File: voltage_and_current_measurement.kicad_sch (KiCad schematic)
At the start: 86 parts, among them IC2 VIA2000SD, J5 V_bat_in, J6 V_bat_out, J7 V_bat_in, J8 V_bat_out, U2 ACS37030LLZATR-065B3, U3 CZ3A05, U4 OPA2328DR, U5 OPA2328DR

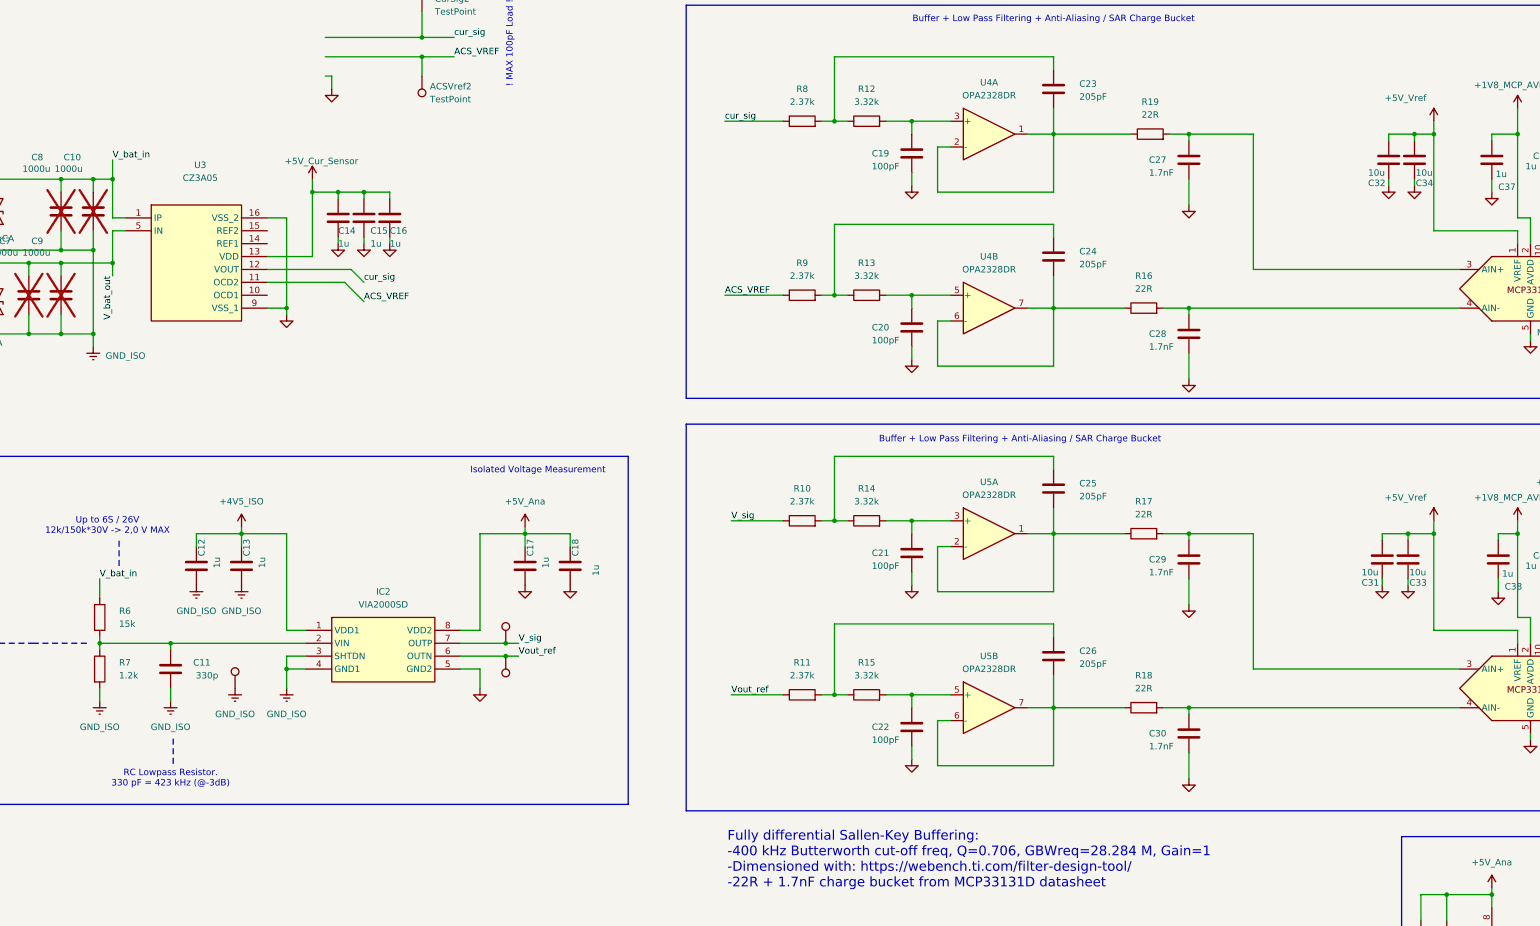
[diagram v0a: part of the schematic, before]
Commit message: Implemented dual SAR ADC Buffering and Current sensor ratiometric supply
[KiCad Version: 10.0.4]
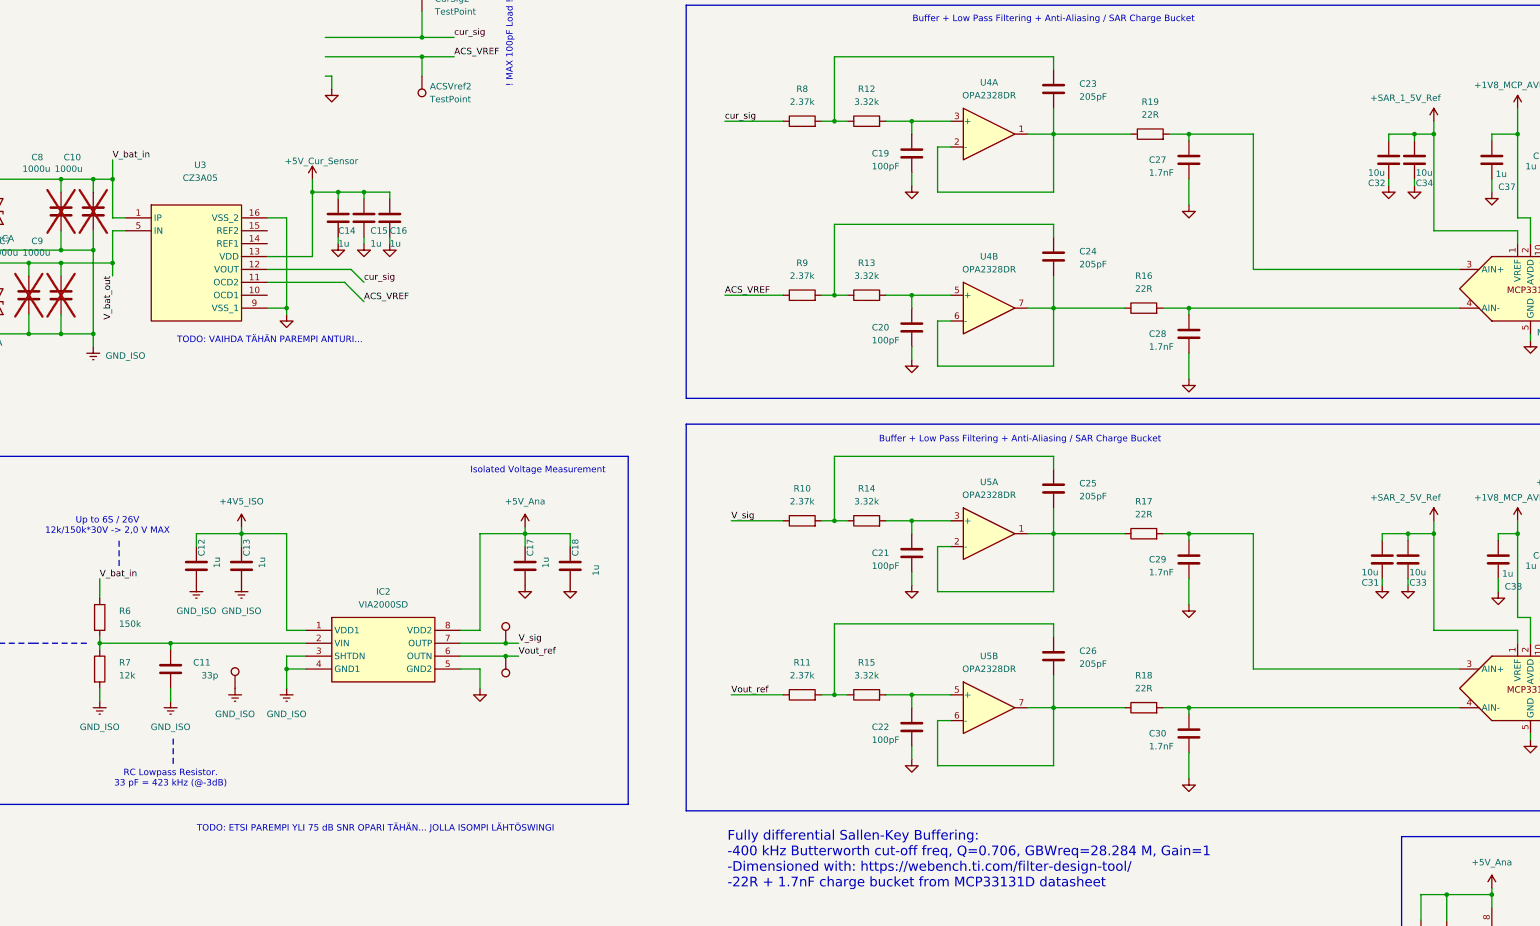
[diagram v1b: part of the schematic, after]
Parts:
- C11: value 330p -> 33p
- R6: value 15k -> 150k
- R7: value 1.2k -> 12k
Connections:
- net +5V_Vref renamed +SAR_1_5V_Ref
- net +SAR_1_5V_Ref: no longer C31.1, C33.1, MCP2.1 (VREF)
- new net +SAR_2_5V_Ref: C31.1, C33.1, MCP2.1 (VREF)
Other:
- note added: "RC Lowpass Resistor. 33 pF = 423 kHz (@-3dB)"
- note added: "TODO: ETSI PAREMPI YLI 75 dB SNR OPARI TÄHÄN... JOLLA ISOMPI LÄHTÖSWINGI"
- note added: "TODO: VAIHDA TÄHÄN PAREMPI ANTURI..."
- note removed: "RC Lowpass Resistor. 330 pF = 423 kHz (@-3dB)"
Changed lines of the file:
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@@
 		)
 	)
-	(text "RC Lowpass Resistor.\n330 pF = 423 kHz (@-3dB)\n"
+	(text "RC Lowpass Resistor.\n33 pF = 423 kHz (@-3dB)\n"
 		(exclude_from_sim no)
 		(at 77.47 193.04 0)
@@
 		)
 	)
+	(text "TODO: VAIHDA TÄHÄN PAREMPI ANTURI..."
+		(exclude_from_sim no)
+		(at 97.028 106.68 0)
+		(effects
+			(font
+				(size 1.27 1.27)
+			)
+		)
+	)
 	(text "Up to 6S / 26V\n12k/150k*30V -> 2,0 V MAX"
 		(exclude_from_sim no)
@@
 		)
 	)
+	(text "TODO: ETSI PAREMPI YLI 75 dB SNR OPARI TÄHÄN... JOLLA ISOMPI LÄHTÖSWINGI"
+		(exclude_from_sim no)
+		(at 117.856 202.946 0)
+		(effects
+			(font
+				(size 1.27 1.27)
+			)
+		)
+	)
 	(text "! MAX 100pF Load !"
 		(exclude_from_sim no)
@@
 	(symbol
 		(lib_id "power:+3V3")
-		(at 326.39 142.24 0)
+		(at 326.39 63.5 0)
 		(unit 1)
 		(body_style 1)
@@
 		(in_pos_files yes)
 		(dnp no)
-		(property "Reference" "#PWR048"
-			(at 326.39 146.05 0)
+		(property "Reference" "#PWR047"
+			(at 326.39 67.31 0)
 			(hide yes)
 			(show_name no)
@@
 			)
 		)
-		(property "Value" "+5V_Vref"
-			(at 320.802 137.668 0)
+		(property "Value" "+SAR_1_5V_Ref"
+			(at 320.802 58.928 0)
 			(show_name no)
 			(do_not_autoplace no)
@@
 		)
 		(property "Footprint" ""
-			(at 326.39 142.24 0)
+			(at 326.39 63.5 0)
 			(hide yes)
 			(show_name no)
@@
 		)
 		(property "Datasheet" ""
-			(at 326.39 142.24 0)
+			(at 326.39 63.5 0)
 			(hide yes)
 			(show_name no)
@@
 		)
 		(property "Description" "Power symbol creates a global label with name \"+3V3\""
-			(at 326.39 142.24 0)
+			(at 326.39 63.5 0)
 			(hide yes)
 			(show_name no)
@@
 			(project "motor_testbench_v1_0"
 				(path "/da638649-102c-44f9-b928-e91cd399cc2f/2da1fd24-7545-4e4a-b589-72e0f66a31f4"
-					(reference "#PWR048")
+					(reference "#PWR047")
 					(unit 1)
 				)
@@
 			)
 		)
-		(property "Value" "330p"
+		(property "Value" "33p"
 			(at 86.868 172.72 0)
 			(show_name no)
@@
 			)
 		)
-		(property "Value" "1.2k"
+		(property "Value" "12k"
 			(at 67.31 172.7199 0)
 			(show_name no)
@@
 	)
 	(symbol
-		(lib_id "power:+3V3")
-		(at 326.39 63.5 0)
-		(unit 1)
-		(body_style 1)
-		(exclude_from_sim no)
-		(in_bom yes)
-		(on_board yes)
-		(in_pos_files yes)
-		(dnp no)
-		(property "Reference" "#PWR047"
-			(at 326.39 67.31 0)
-			(hide yes)
-			(show_name no)
-			(do_not_autoplace no)
-			(effects
-				(font
-					(size 1.27 1.27)
-				)
-			)
-		)
-		(property "Value" "+5V_Vref"
-			(at 320.802 58.928 0)
-			(show_name no)
-			(do_not_autoplace no)
-			(effects
-				(font
-					(size 1.27 1.27)
-				)
-			)
-		)
-		(property "Footprint" ""
-			(at 326.39 63.5 0)
-			(hide yes)
-			(show_name no)
-			(do_not_autoplace no)
-			(effects
-				(font
-					(size 1.27 1.27)
-				)
-			)
-		)
-		(property "Datasheet" ""
-			(at 326.39 63.5 0)
-			(hide yes)
-			(show_name no)
-			(do_not_autoplace no)
-			(effects
-				(font
-					(size 1.27 1.27)
-				)
-			)
-		)
-		(property "Description" "Power symbol creates a global label with name \"+3V3\""
-			(at 326.39 63.5 0)
-			(hide yes)
-			(show_name no)
-			(do_not_autoplace no)
-			(effects
-				(font
-					(size 1.27 1.27)
-				)
-			)
-		)
-		(pin "1"
-		)
-		(instances
-			(project "motor_testbench_v1_0"
-				(path "/da638649-102c-44f9-b928-e91cd399cc2f/2da1fd24-7545-4e4a-b589-72e0f66a31f4"
-					(reference "#PWR047")
-					(unit 1)
-				)
-			)
-		)
-	)
-	(symbol
 		(lib_id "Device:C")
 		(at -40.64 43.18 0)
@@
 			)
 		)
-		(property "Value" "15k"
+		(property "Value" "150k"
 			(at 67.31 162.5599 0)
 			(show_name no)
@@
 					(unit 1)
 				)
+			)
+		)
+	)
+	(symbol
+		(lib_id "power:+3V3")
+		(at 326.39 142.24 0)
+		(unit 1)
+		(body_style 1)
+		(exclude_from_sim no)
+		(in_bom yes)
+		(on_board yes)
+		(in_pos_files yes)
+		(dnp no)
+		(property "Reference" "#PWR048"
+			(at 326.39 146.05 0)
+			(hide yes)
+			(show_name no)
+			(do_not_autoplace no)
+			(effects
+				(font
+					(size 1.27 1.27)
+				)
+			)
+		)
+		(property "Value" "+SAR_2_5V_Ref"
+			(at 320.802 137.668 0)
+			(show_name no)
+			(do_not_autoplace no)
+			(effects
+				(font
+					(size 1.27 1.27)
+				)
+			)
+		)
+		(property "Footprint" ""
+			(at 326.39 142.24 0)
+			(hide yes)
+			(show_name no)
+			(do_not_autoplace no)
+			(effects
+				(font
+					(size 1.27 1.27)
+				)
+			)
+		)
+		(property "Datasheet" ""
+			(at 326.39 142.24 0)
+			(hide yes)
+			(show_name no)
+			(do_not_autoplace no)
+			(effects
+				(font
+					(size 1.27 1.27)
+				)
+			)
+		)
+		(property "Description" "Power symbol creates a global label with name \"+3V3\""
+			(at 326.39 142.24 0)
+			(hide yes)
+			(show_name no)
+			(do_not_autoplace no)
+			(effects
+				(font
+					(size 1.27 1.27)
+				)
+			)
+		)
+		(pin "1"
+		)
+		(instances
+			(project "motor_testbench_v1_0"
+				(path "/da638649-102c-44f9-b928-e91cd399cc2f/2da1fd24-7545-4e4a-b589-72e0f66a31f4"
+					(reference "#PWR048")
+					(unit 1)
+				)

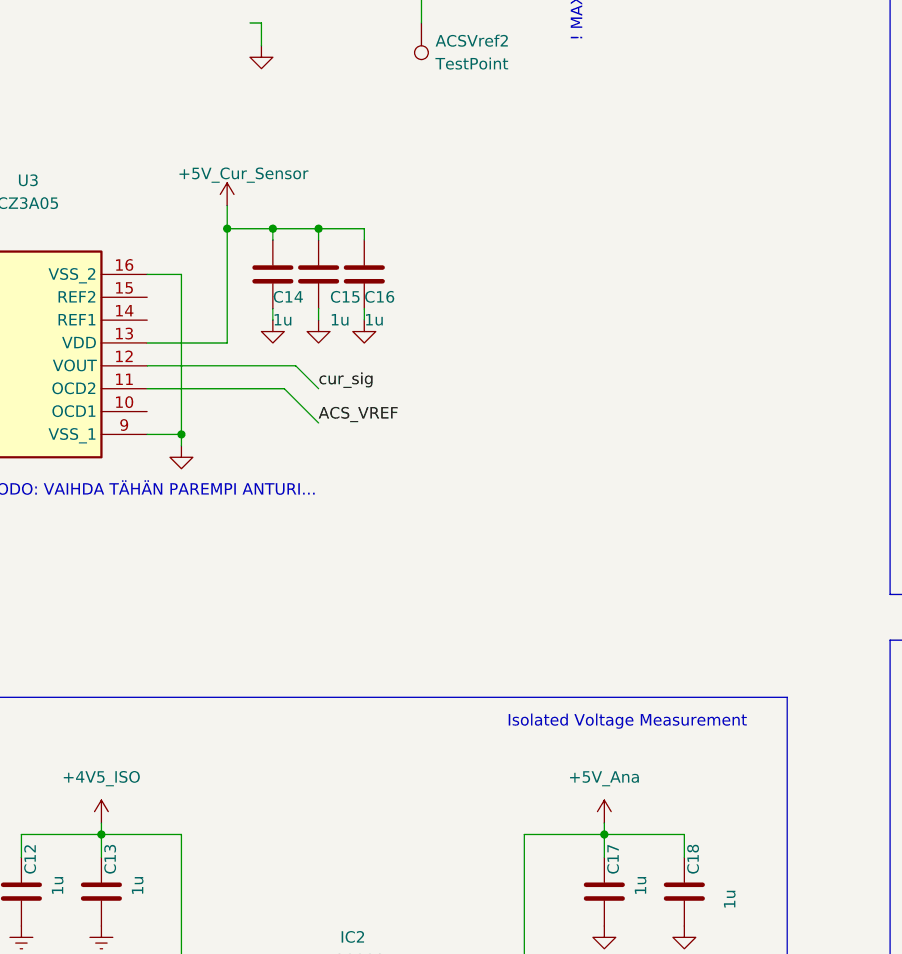
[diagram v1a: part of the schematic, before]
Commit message: Improved NTC measurements, improved layout. Added proper startup sequence for the power stages.
[KiCad Version: 10.0.4]
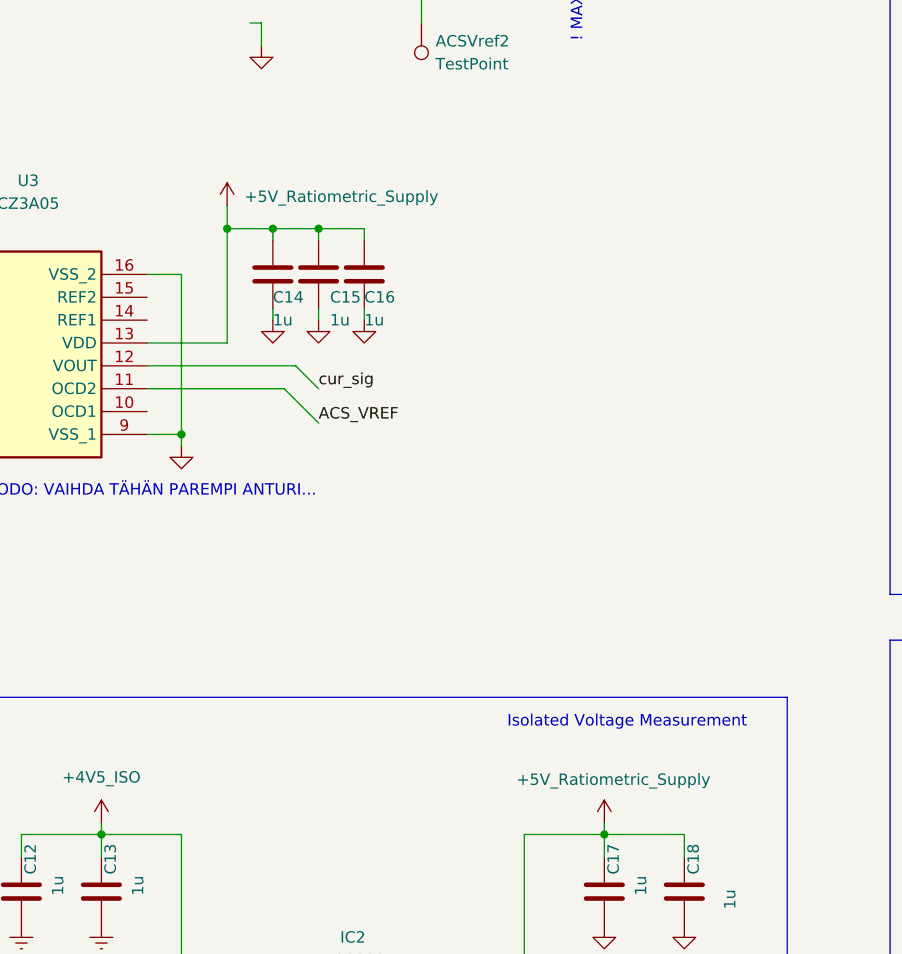
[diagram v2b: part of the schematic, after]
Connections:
- net +5V_Ana: no longer C17.1, C18.1, IC2.8 (VDD2)
- net +5V_Cur_Sensor renamed +5V_Ratiometric_Supply
- net +5V_Ratiometric_Supply: now also C17.1, C18.1, IC2.8 (VDD2)
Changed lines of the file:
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@@
 	)
 	(symbol
-		(lib_id "power:+3V3")
-		(at 147.32 143.51 0)
-		(unit 1)
-		(body_style 1)
-		(exclude_from_sim no)
-		(in_bom yes)
-		(on_board yes)
-		(in_pos_files yes)
-		(dnp no)
-		(property "Reference" "#PWR031"
-			(at 147.32 147.32 0)
-			(hide yes)
-			(show_name no)
-			(do_not_autoplace no)
-			(effects
-				(font
-					(size 1.27 1.27)
-				)
-			)
-		)
-		(property "Value" "+5V_Ana"
-			(at 147.32 138.43 0)
-			(show_name no)
-			(do_not_autoplace no)
-			(effects
-				(font
-					(size 1.27 1.27)
-				)
-			)
-		)
-		(property "Footprint" ""
-			(at 147.32 143.51 0)
-			(hide yes)
-			(show_name no)
-			(do_not_autoplace no)
-			(effects
-				(font
-					(size 1.27 1.27)
-				)
-			)
-		)
-		(property "Datasheet" ""
-			(at 147.32 143.51 0)
-			(hide yes)
-			(show_name no)
-			(do_not_autoplace no)
-			(effects
-				(font
-					(size 1.27 1.27)
-				)
-			)
-		)
-		(property "Description" "Power symbol creates a global label with name \"+3V3\""
-			(at 147.32 143.51 0)
-			(hide yes)
-			(show_name no)
-			(do_not_autoplace no)
-			(effects
-				(font
-					(size 1.27 1.27)
-				)
-			)
-		)
-		(pin "1"
-		)
-		(instances
-			(project "motor_testbench_v1_0"
-				(path "/da638649-102c-44f9-b928-e91cd399cc2f/2da1fd24-7545-4e4a-b589-72e0f66a31f4"
-					(reference "#PWR031")
-					(unit 1)
-				)
-			)
-		)
-	)
-	(symbol
 		(lib_id "Connector:TestPoint")
 		(at 365.76 163.83 0)
@@
 	)
 	(symbol
+		(lib_id "power:+3V3")
+		(at 105.41 74.93 0)
+		(unit 1)
+		(body_style 1)
+		(exclude_from_sim no)
+		(in_bom yes)
+		(on_board yes)
+		(in_pos_files yes)
+		(dnp no)
+		(property "Reference" "#PWR025"
+			(at 105.41 78.74 0)
+			(hide yes)
+			(show_name no)
+			(do_not_autoplace no)
+			(effects
+				(font
+					(size 1.27 1.27)
+				)
+			)
+		)
+		(property "Value" "+5V_Ratiometric_Supply"
+			(at 118.11 73.914 0)
+			(show_name no)
+			(do_not_autoplace no)
+			(effects
+				(font
+					(size 1.27 1.27)
+				)
+			)
+		)
+		(property "Footprint" ""
+			(at 105.41 74.93 0)
+			(hide yes)
+			(show_name no)
+			(do_not_autoplace no)
+			(effects
+				(font
+					(size 1.27 1.27)
+				)
+			)
+		)
+		(property "Datasheet" ""
+			(at 105.41 74.93 0)
+			(hide yes)
+			(show_name no)
+			(do_not_autoplace no)
+			(effects
+				(font
+					(size 1.27 1.27)
+				)
+			)
+		)
+		(property "Description" "Power symbol creates a global label with name \"+3V3\""
+			(at 105.41 74.93 0)
+			(hide yes)
+			(show_name no)
+			(do_not_autoplace no)
+			(effects
+				(font
+					(size 1.27 1.27)
+				)
+			)
+		)
+		(pin "1"
+		)
+		(instances
+			(project "motor_testbench_v1_0"
+				(path "/da638649-102c-44f9-b928-e91cd399cc2f/2da1fd24-7545-4e4a-b589-72e0f66a31f4"
+					(reference "#PWR025")
+					(unit 1)
+				)
+			)
+		)
+	)
+	(symbol
 		(lib_id "power:GND")
 		(at -40.64 48.26 0)
@@
 	)
 	(symbol
+		(lib_id "power:+3V3")
+		(at 147.32 143.51 0)
+		(unit 1)
+		(body_style 1)
+		(exclude_from_sim no)
+		(in_bom yes)
+		(on_board yes)
+		(in_pos_files yes)
+		(dnp no)
+		(property "Reference" "#PWR031"
+			(at 147.32 147.32 0)
+			(hide yes)
+			(show_name no)
+			(do_not_autoplace no)
+			(effects
+				(font
+					(size 1.27 1.27)
+				)
+			)
+		)
+		(property "Value" "+5V_Ratiometric_Supply"
+			(at 148.336 138.684 0)
+			(show_name no)
+			(do_not_autoplace no)
+			(effects
+				(font
+					(size 1.27 1.27)
+				)
+			)
+		)
+		(property "Footprint" ""
+			(at 147.32 143.51 0)
+			(hide yes)
+			(show_name no)
+			(do_not_autoplace no)
+			(effects
+				(font
+					(size 1.27 1.27)
+				)
+			)
+		)
+		(property "Datasheet" ""
+			(at 147.32 143.51 0)
+			(hide yes)
+			(show_name no)
+			(do_not_autoplace no)
+			(effects
+				(font
+					(size 1.27 1.27)
+				)
+			)
+		)
+		(property "Description" "Power symbol creates a global label with name \"+3V3\""
+			(at 147.32 143.51 0)
+			(hide yes)
+			(show_name no)
+			(do_not_autoplace no)
+			(effects
+				(font
+					(size 1.27 1.27)
+				)
+			)
+		)
+		(pin "1"
+		)
+		(instances
+			(project "motor_testbench_v1_0"
+				(path "/da638649-102c-44f9-b928-e91cd399cc2f/2da1fd24-7545-4e4a-b589-72e0f66a31f4"
+					(reference "#PWR031")
+					(unit 1)
+				)
+			)
+		)
+	)
+	(symbol
 		(lib_id "Amplifier_Operational:OPA2325")
 		(at 340.36 226.06 0)
@@
 					(unit 1)
 				)
-			)
-		)
-	)
-	(symbol
-		(lib_id "power:+3V3")
-		(at 105.41 74.93 0)
-		(unit 1)
-		(body_style 1)
-		(exclude_from_sim no)
-		(in_bom yes)
-		(on_board yes)
-		(in_pos_files yes)
-		(dnp no)
-		(property "Reference" "#PWR025"
-			(at 105.41 78.74 0)
-			(hide yes)
-			(show_name no)
-			(do_not_autoplace no)
-			(effects
-				(font
-					(size 1.27 1.27)
-				)
-			)
-		)
-		(property "Value" "+5V_Cur_Sensor"
-			(at 107.188 71.374 0)
-			(show_name no)
-			(do_not_autoplace no)
-			(effects
-				(font
-					(size 1.27 1.27)
-				)
-			)
-		)
-		(property "Footprint" ""
-			(at 105.41 74.93 0)
-			(hide yes)
-			(show_name no)
-			(do_not_autoplace no)
-			(effects
-				(font
-					(size 1.27 1.27)
-				)
-			)
-		)
-		(property "Datasheet" ""
-			(at 105.41 74.93 0)
-			(hide yes)
-			(show_name no)
-			(do_not_autoplace no)
-			(effects
-				(font
-					(size 1.27 1.27)
-				)
-			)
-		)
-		(property "Description" "Power symbol creates a global label with name \"+3V3\""
-			(at 105.41 74.93 0)
-			(hide yes)
-			(show_name no)
-			(do_not_autoplace no)
-			(effects
-				(font
-					(size 1.27 1.27)
-				)
-			)
-		)
-		(pin "1"
-		)
-		(instances
-			(project "motor_testbench_v1_0"
-				(path "/da638649-102c-44f9-b928-e91cd399cc2f/2da1fd24-7545-4e4a-b589-72e0f66a31f4"
-					(reference "#PWR025")
-					(unit 1)
-				)
